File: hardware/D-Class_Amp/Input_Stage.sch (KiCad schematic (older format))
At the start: 15 parts, among them U11 LM324

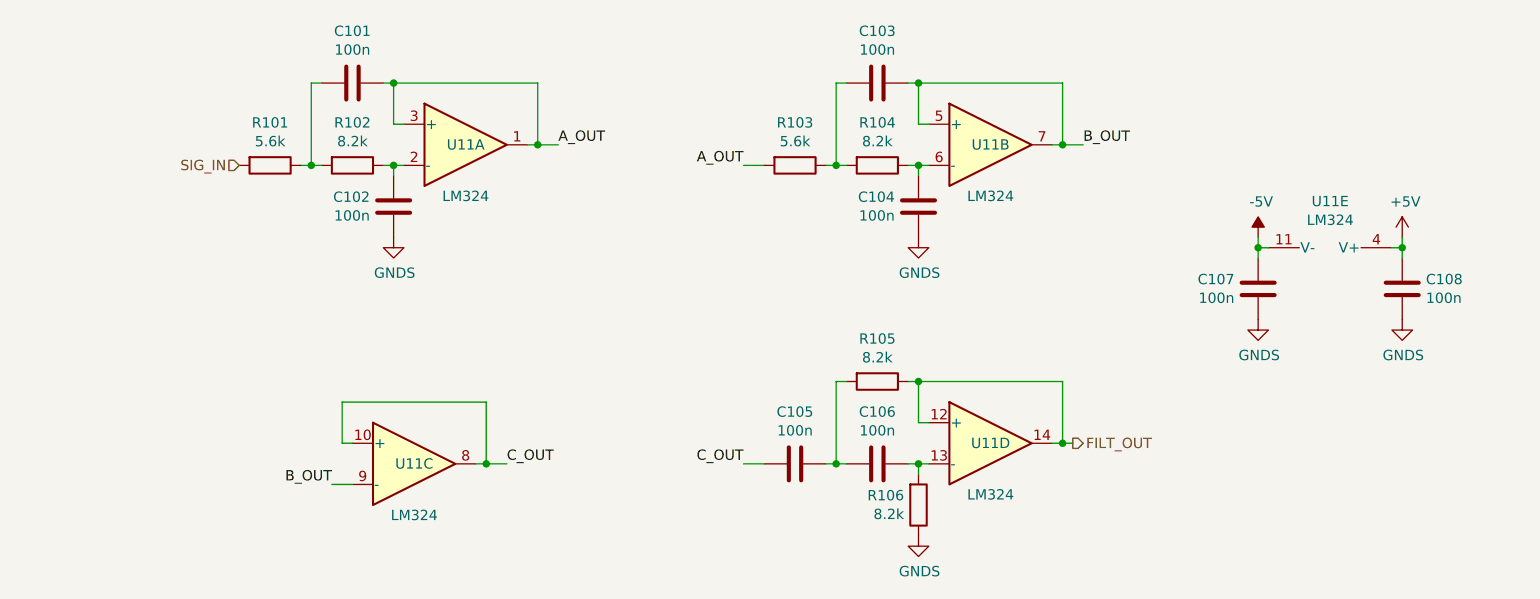
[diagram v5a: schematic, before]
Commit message: Added input bias circuit and gain stage to input-stage schematic.
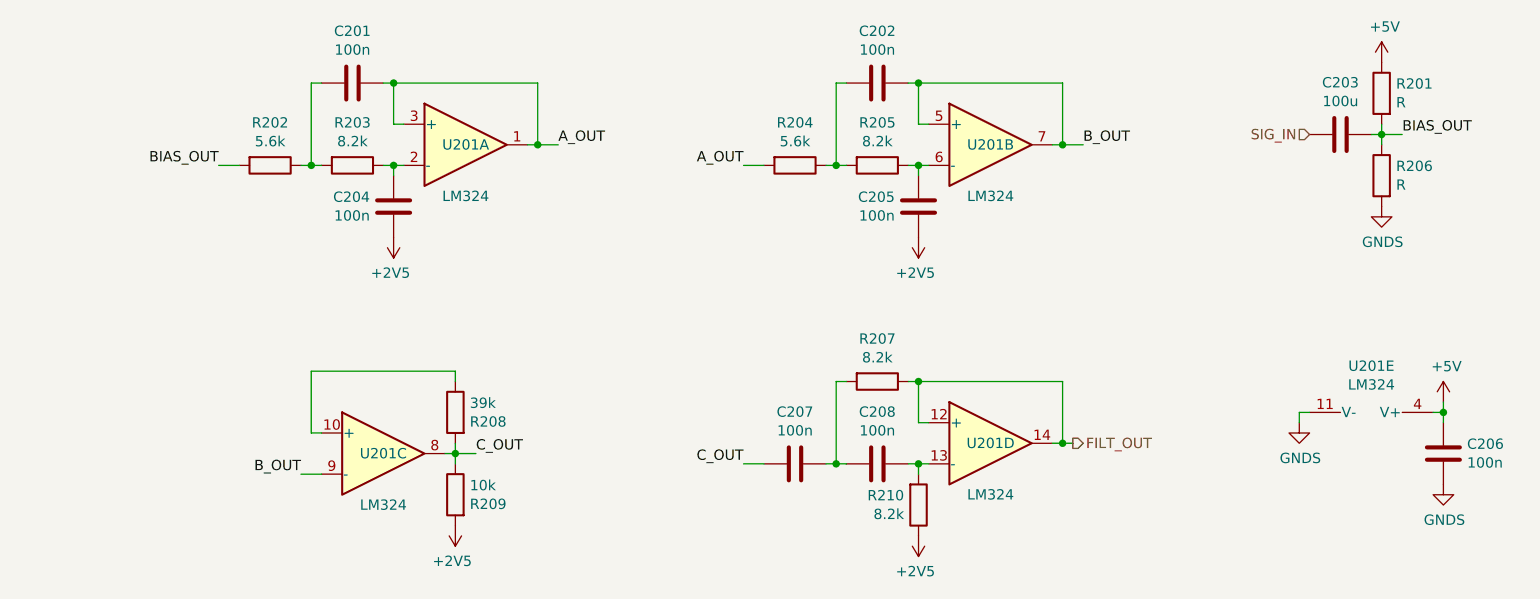
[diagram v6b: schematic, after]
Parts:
- removed C107: 100n, Capacitor_SMD:C_0805_2012Metric_Pad1.18x1.45mm_HandSolder, symbol Device:C
- added C203: 100u, Capacitor_SMD:C_0805_2012Metric_Pad1.18x1.45mm_HandSolder, symbol Device:C
- added R201, R206: R, symbol Device:R
- added R208: 39k, Resistor_SMD:R_0805_2012Metric_Pad1.20x1.40mm_HandSolder, symbol Device:R
- added R209: 10k, Resistor_SMD:R_0805_2012Metric_Pad1.20x1.40mm_HandSolder, symbol Device:R
- renumbered C101 to C201, C103 to C202, C102 to C204, C104 to C205, C108 to C206, C105 to C207, C106 to C208, R101 to R202, R102 to R203, R103 to R204, R104 to R205, R105 to R207, R106 to R210, U11 to U201
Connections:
- net -5V is gone; now on net GNDS: U201.11 (V-)
- net +5V: now also R201.1
- net C_OUT: now also R208.2, R209.1; no longer U201.10 (+)
- net GNDS: now also R206.2; no longer C204.1, C205.1, R210.1
- net SIG_IN: now also C203.2; no longer R202.2
- new net: R208.1, U201.10 (+)
- new net +2V5: C204.1, C205.1, R209.2, R210.1
- new net BIAS_OUT: C203.1, R201.2, R202.2, R206.1
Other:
- moved on the sheet: C206, U201C, U201E

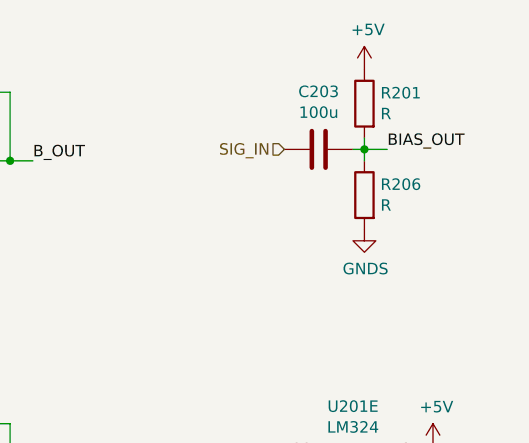
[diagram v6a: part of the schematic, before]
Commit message: added resistor values
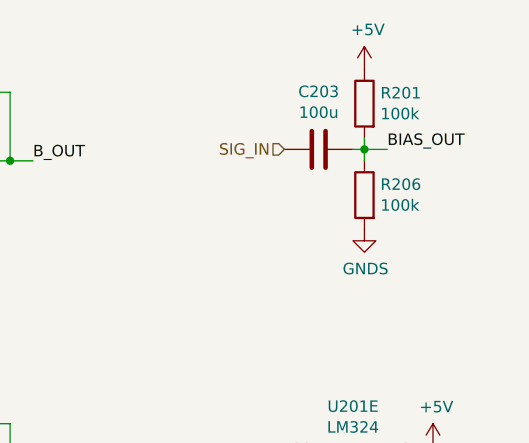
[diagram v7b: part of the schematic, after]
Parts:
- R201, R206: value R -> 100k
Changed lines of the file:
@@
 P 8150 3250
 F 0 "R206" H 8080 3296 50  0000 R CNN
-F 1 "R" H 8080 3205 50  0000 R CNN
+F 1 "100k" H 8080 3205 50  0000 R CNN
 F 2 "" V 8080 3250 50  0001 C CNN
 F 3 "~" H 8150 3250 50  0001 C CNN
@@
 P 8150 2850
 F 0 "R201" H 8080 2896 50  0000 R CNN
-F 1 "R" H 8080 2805 50  0000 R CNN
+F 1 "100k" H 8080 2805 50  0000 R CNN
 F 2 "" V 8080 2850 50  0001 C CNN
 F 3 "~" H 8150 2850 50  0001 C CNN

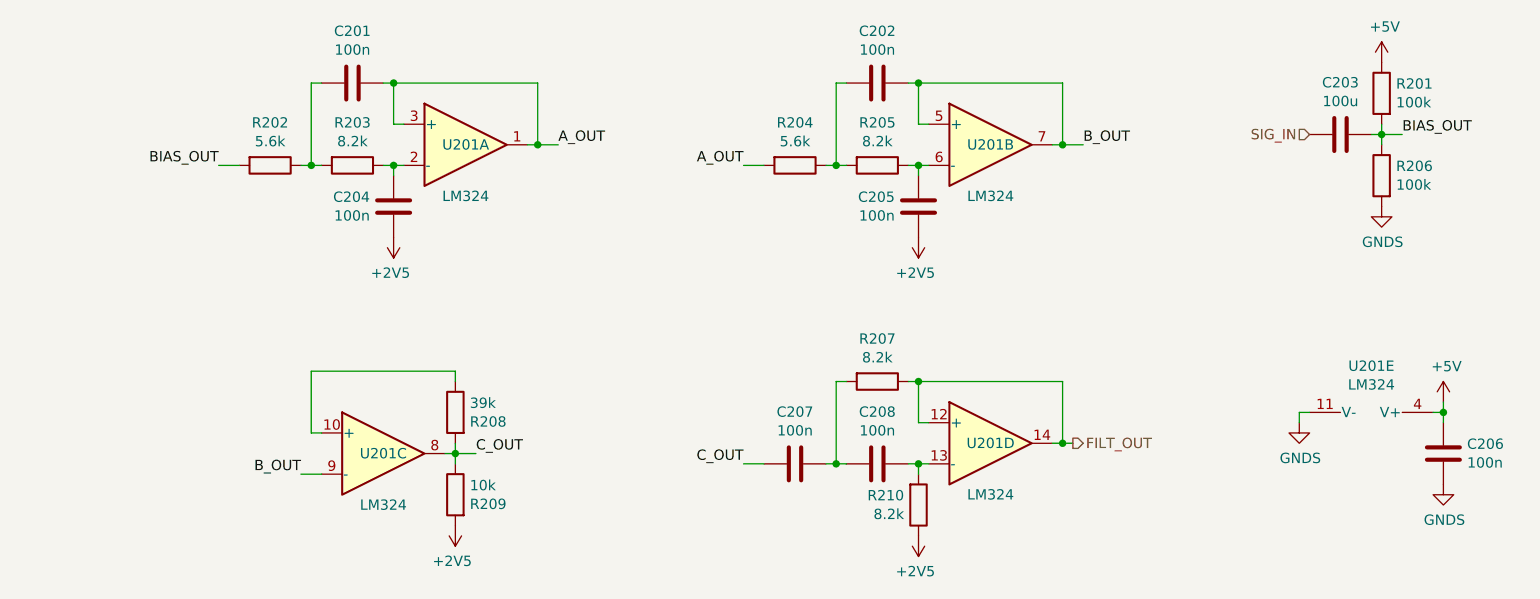
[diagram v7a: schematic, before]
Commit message: updated input stage schematic
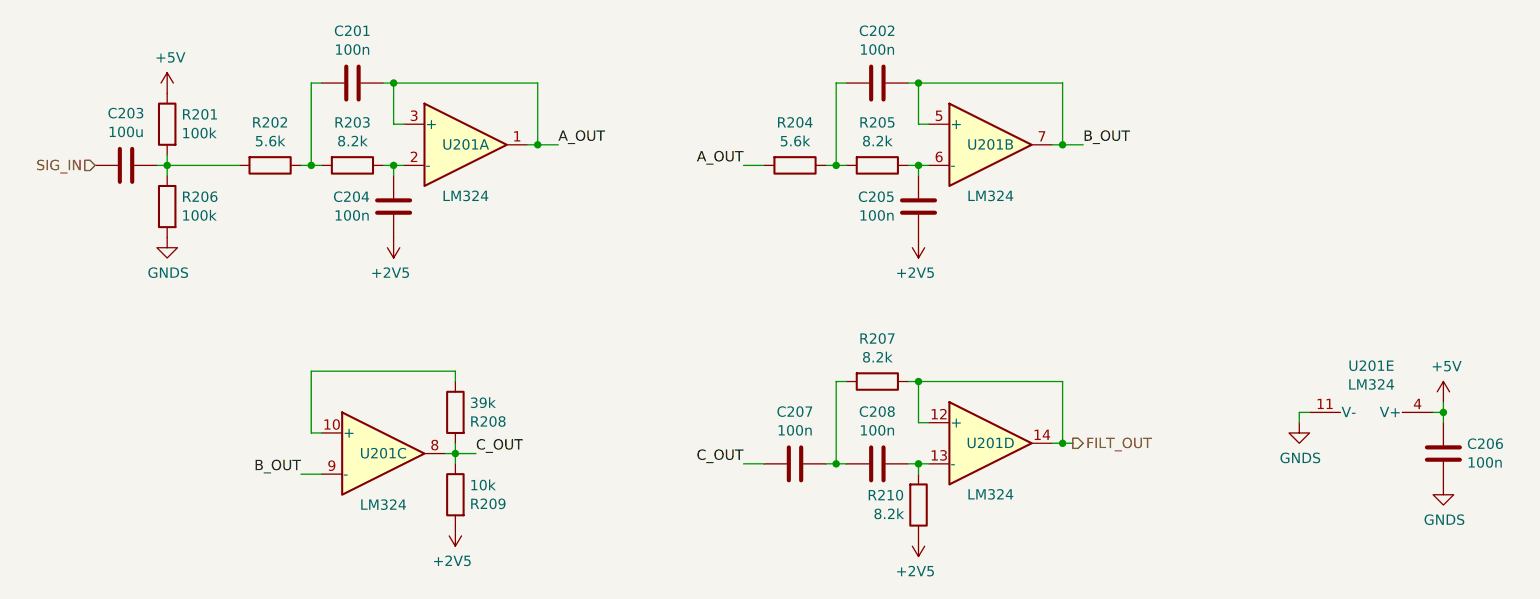
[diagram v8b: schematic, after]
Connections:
- net BIAS_OUT: no longer names the net of C203.1, R201.2, R202.2, R206.1
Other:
- moved on the sheet: C203, R201, R206
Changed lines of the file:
@@
 	8450 4400 8450 4350
 Connection ~ 8450 4400
-Text HLabel 7800 3050 0    50   Input ~ 0
+Text HLabel 1900 3200 0    50   Input ~ 0
 SIG_IN
 Wire Wire Line
@@
 L power:GNDS #PWR0202
 U 1 1 610B63BB
-P 8150 3400
-F 0 "#PWR0202" H 8150 3150 50  0001 C CNN
-F 1 "GNDS" H 8155 3227 50  0000 C CNN
-F 2 "" H 8150 3400 50  0001 C CNN
-F 3 "" H 8150 3400 50  0001 C CNN
-	1    8150 3400
+P 2250 3550
+F 0 "#PWR0202" H 2250 3300 50  0001 C CNN
+F 1 "GNDS" H 2255 3377 50  0000 C CNN
+F 2 "" H 2250 3550 50  0001 C CNN
+F 3 "" H 2250 3550 50  0001 C CNN
+	1    2250 3550
 	1    0    0    -1
 $EndComp
@@
 L power:+5V #PWR0201
 U 1 1 610B76DD
-P 8150 2700
-F 0 "#PWR0201" H 8150 2550 50  0001 C CNN
-F 1 "+5V" H 8165 2873 50  0000 C CNN
-F 2 "" H 8150 2700 50  0001 C CNN
-F 3 "" H 8150 2700 50  0001 C CNN
-	1    8150 2700
+P 2250 2850
+F 0 "#PWR0201" H 2250 2700 50  0001 C CNN
+F 1 "+5V" H 2265 3023 50  0000 C CNN
+F 2 "" H 2250 2850 50  0001 C CNN
+F 3 "" H 2250 2850 50  0001 C CNN
+	1    2250 2850
 	1    0    0    -1
 $EndComp
@@
 L Device:R R206
 U 1 1 610B8ECE
-P 8150 3250
-F 0 "R206" H 8080 3296 50  0000 R CNN
-F 1 "100k" H 8080 3205 50  0000 R CNN
-F 2 "" V 8080 3250 50  0001 C CNN
-F 3 "~" H 8150 3250 50  0001 C CNN
-	1    8150 3250
+P 2250 3400
+F 0 "R206" H 2180 3446 50  0000 R CNN
+F 1 "100k" H 2180 3355 50  0000 R CNN
+F 2 "" V 2180 3400 50  0001 C CNN
+F 3 "~" H 2250 3400 50  0001 C CNN
+	1    2250 3400
 	-1   0    0    -1
 $EndComp
@@
 L Device:R R201
 U 1 1 610BCA88
-P 8150 2850
-F 0 "R201" H 8080 2896 50  0000 R CNN
-F 1 "100k" H 8080 2805 50  0000 R CNN
-F 2 "" V 8080 2850 50  0001 C CNN
-F 3 "~" H 8150 2850 50  0001 C CNN
-	1    8150 2850
+P 2250 3000
+F 0 "R201" H 2180 3046 50  0000 R CNN
+F 1 "100k" H 2180 2955 50  0000 R CNN
+F 2 "" V 2180 3000 50  0001 C CNN
+F 3 "~" H 2250 3000 50  0001 C CNN
+	1    2250 3000
 	-1   0    0    -1
 $EndComp
@@
 L Device:C C203
 U 1 1 610C2C53
-P 7950 3050
-F 0 "C203" V 7698 3050 50  0000 C CNN
-F 1 "100u" V 7789 3050 50  0000 C CNN
-F 2 "Capacitor_SMD:C_0805_2012Metric_Pad1.18x1.45mm_HandSolder" H 7988 2900 50  0001 C CNN
-F 3 "~" H 7950 3050 50  0001 C CNN
-	1    7950 3050
+P 2050 3200
+F 0 "C203" V 1798 3200 50  0000 C CNN
+F 1 "100u" V 1889 3200 50  0000 C CNN
+F 2 "Capacitor_SMD:C_0805_2012Metric_Pad1.18x1.45mm_HandSolder" H 2088 3050 50  0001 C CNN
+F 3 "~" H 2050 3200 50  0001 C CNN
+	1    2050 3200
 	0    1    1    0
 $EndComp
 Wire Wire Line
-	8150 3000 8150 3050
-Text Label 2500 3200 2    50   ~ 0
-BIAS_OUT
-Wire Wire Line
-	2500 3200 2600 3200
-Wire Wire Line
-	8100 3050 8150 3050
-Connection ~ 8150 3050
-Wire Wire Line
-	8150 3050 8150 3100
-Text Label 8250 3050 0    50   ~ 0
-BIAS_OUT
-Wire Wire Line
-	8250 3050 8150 3050
+	2250 3150 2250 3200
+Wire Wire Line
+	2200 3200 2250 3200
+Connection ~ 2250 3200
+Wire Wire Line
+	2250 3200 2250 3250
 Wire Wire Line
 	3600 4600 3650 4600
@@
 	-1   0    0    1
 $EndComp
+Wire Wire Line
+	2250 3200 2600 3200
 $EndSCHEMATC
